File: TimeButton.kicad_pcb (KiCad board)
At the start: 2 copper layers, 3 parts, among them P1 USB_C_Plug_USB2.0, U1 PIC18F15Q41-I/SS, U2 FT231XS

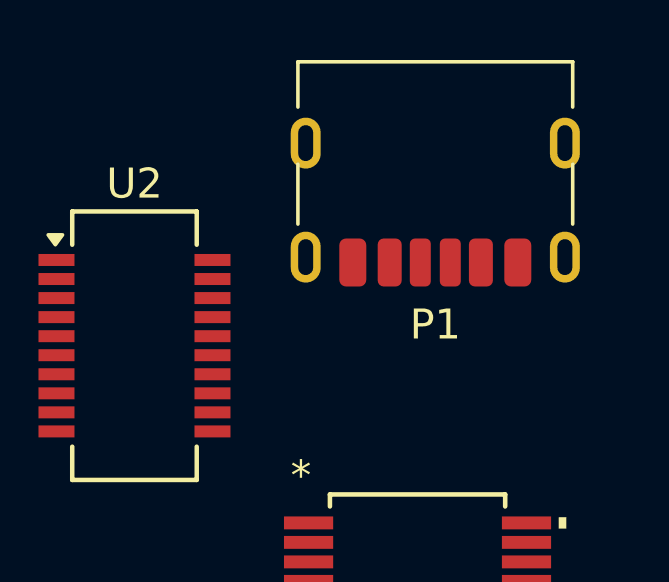
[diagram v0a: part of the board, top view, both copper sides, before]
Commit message: Changed USB_C connector from 6Pin to 16Pin
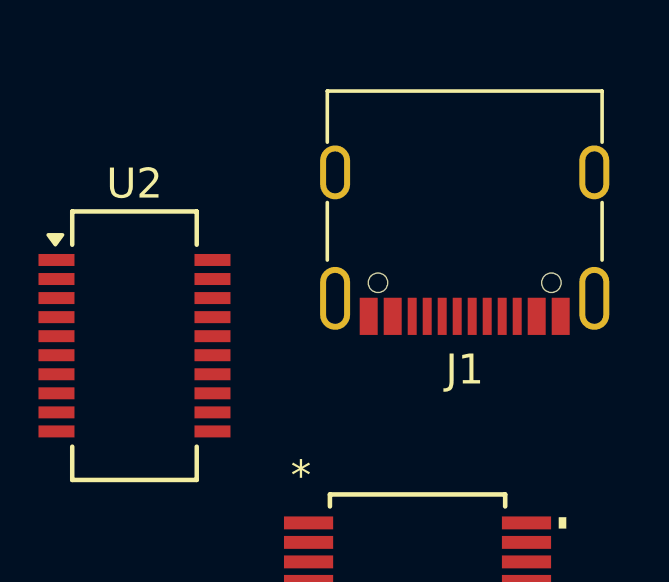
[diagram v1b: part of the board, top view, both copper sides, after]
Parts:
- removed P1: USB_C_Plug_USB2.0, Connector_USB:USB_C_Receptacle_HRO_TYPE-C-31-M-17
- added J1: USB_C_Receptacle_USB2.0_16P, Connector_USB:USB_C_Receptacle_G-Switch_GT-USB-7010ASV, F.Cu at (42.5, 30.3)

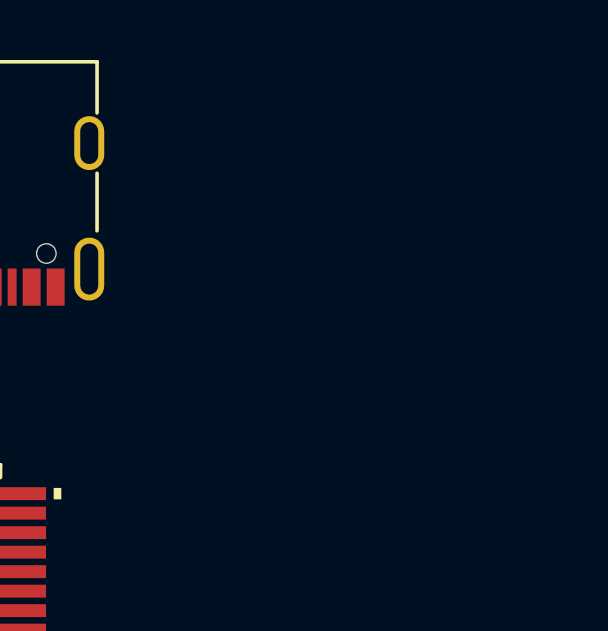
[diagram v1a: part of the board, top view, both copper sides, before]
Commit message: Added LEDs
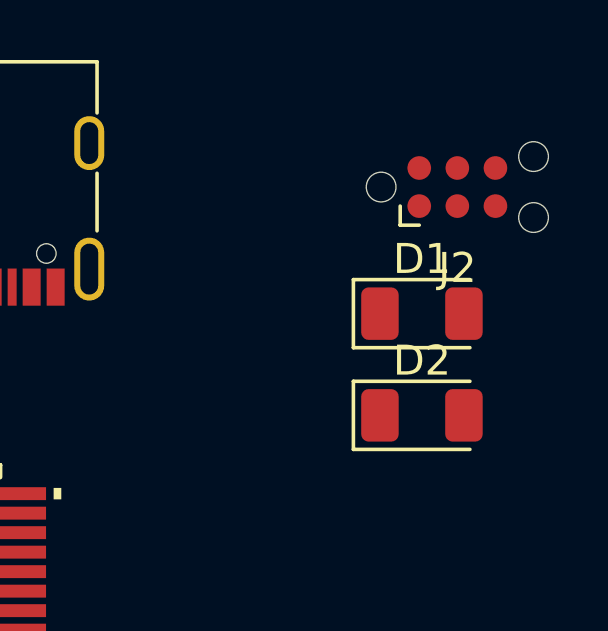
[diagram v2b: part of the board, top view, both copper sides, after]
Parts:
- added D1: 0603-Blue, LED_SMD:LED_1206_3216Metric, F.Cu at (57.9, 34.9)
- added D2: 0603-Green, LED_SMD:LED_1206_3216Metric, F.Cu at (57.9, 38.3)
- added J2: Conn_ARM_SWD_TagConnect_TC2030-NL, Connector:Tag-Connect_TC2030-IDC-NL_2x03_P1.27mm_Vertical, F.Cu at (59.1, 30.7)

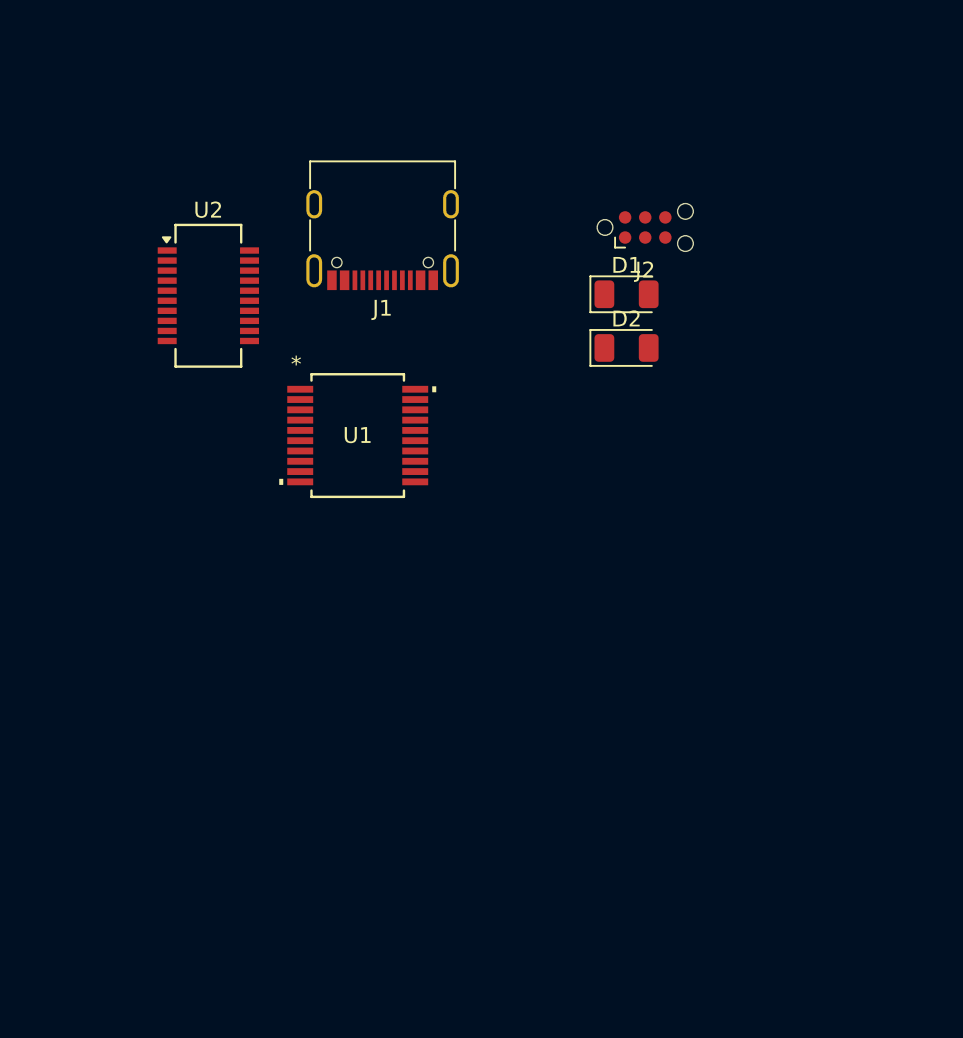
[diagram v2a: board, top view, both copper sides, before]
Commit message: Added TagConnect connections in the schematic
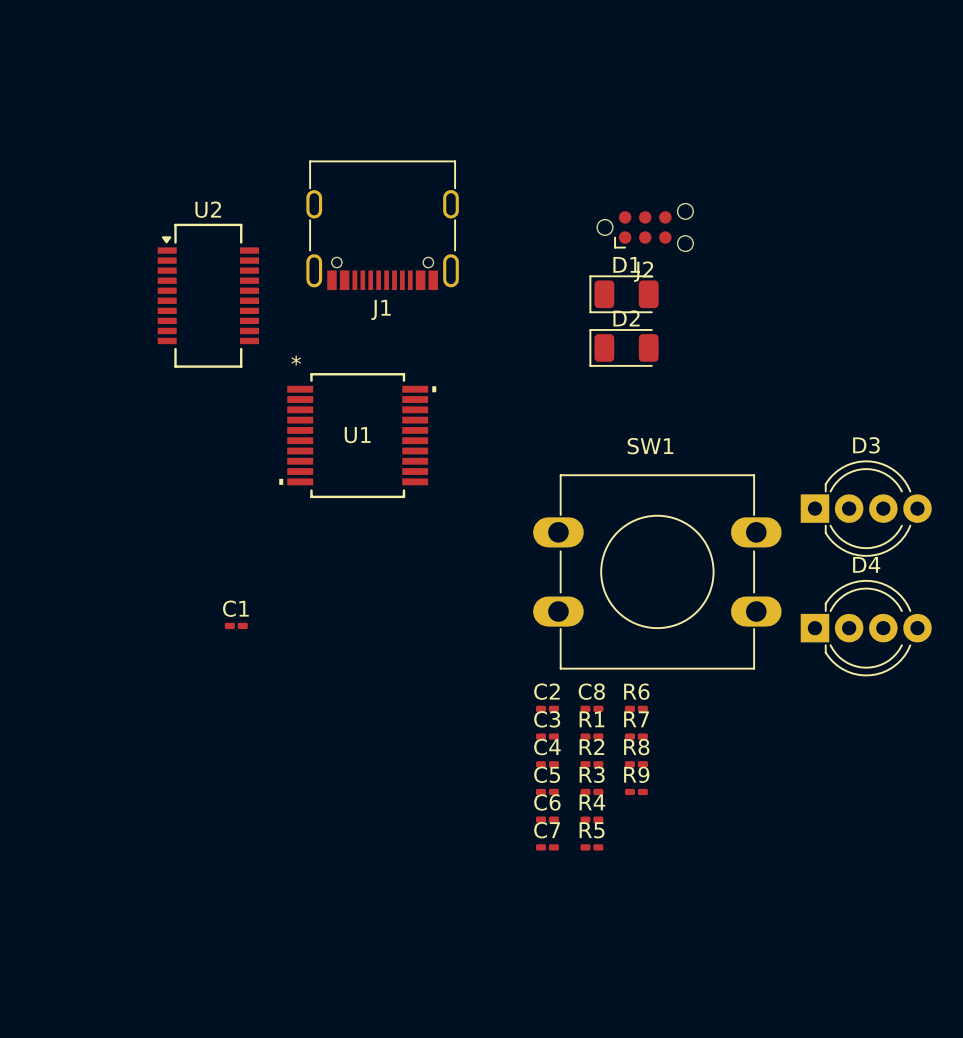
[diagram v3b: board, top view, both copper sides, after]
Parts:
- added C1: 10nF, Capacitor_SMD:C_0201_0603Metric_Pad0.64x0.40mm_HandSolder, F.Cu at (33.2, 55.9)
- added C2: 4.7uF, Capacitor_SMD:C_0201_0603Metric_Pad0.64x0.40mm_HandSolder, F.Cu at (52.9, 61.1)
- added C3: 10nF, Capacitor_SMD:C_0201_0603Metric_Pad0.64x0.40mm_HandSolder, F.Cu at (52.9, 62.9)
- added C4: 100nF, Capacitor_SMD:C_0201_0603Metric_Pad0.64x0.40mm_HandSolder, F.Cu at (52.9, 64.6)
- added C5: 4.7uF, Capacitor_SMD:C_0201_0603Metric_Pad0.64x0.40mm_HandSolder, F.Cu at (52.9, 66.4)
- added C6: 4.7uF, Capacitor_SMD:C_0201_0603Metric_Pad0.64x0.40mm_HandSolder, F.Cu at (52.9, 68.1)
- added C7: 100nF, Capacitor_SMD:C_0201_0603Metric_Pad0.64x0.40mm_HandSolder, F.Cu at (52.9, 69.9)
- added C8: 10nF, Capacitor_SMD:C_0201_0603Metric_Pad0.64x0.40mm_HandSolder, F.Cu at (55.7, 61.1)
- added D3: LED_RAGB, LED_THT:LED_D5.0mm-4_RGB_Wide_Pins, F.Cu at (69.8, 48.5)
- added D4: LED_RAGB, LED_THT:LED_D5.0mm-4_RGB_Wide_Pins, F.Cu at (69.8, 56.0)
- added R1: 10k, Resistor_SMD:R_0201_0603Metric_Pad0.64x0.40mm_HandSolder, F.Cu at (55.7, 62.9)
- added R2: 5.1k, Resistor_SMD:R_0201_0603Metric_Pad0.64x0.40mm_HandSolder, F.Cu at (55.7, 64.6)
- added R3: 27R, Resistor_SMD:R_0201_0603Metric_Pad0.64x0.40mm_HandSolder, F.Cu at (55.7, 66.4)
- added R4: 27R, Resistor_SMD:R_0201_0603Metric_Pad0.64x0.40mm_HandSolder, F.Cu at (55.7, 68.1)
- added R5: 1M, Resistor_SMD:R_0201_0603Metric_Pad0.64x0.40mm_HandSolder, F.Cu at (55.7, 69.9)
- added R6: 5.1k, Resistor_SMD:R_0201_0603Metric_Pad0.64x0.40mm_HandSolder, F.Cu at (58.5, 61.1)
- added R7: 100R, Resistor_SMD:R_0201_0603Metric_Pad0.64x0.40mm_HandSolder, F.Cu at (58.5, 62.9)
- added R8: 50R, Resistor_SMD:R_0201_0603Metric_Pad0.64x0.40mm_HandSolder, F.Cu at (58.5, 64.6)
- added R9: 50R, Resistor_SMD:R_0201_0603Metric_Pad0.64x0.40mm_HandSolder, F.Cu at (58.5, 66.4)
- added SW1: SW_Push, Button_Switch_THT:SW_PUSH-12mm, F.Cu at (53.6, 50.0)
- J2: value Conn_ARM_SWD_TagConnect_TC2030-NL -> TagConnect
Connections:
- J2 pad 1: unconnected-(J2-VCC-Pad1) -> 5V
- J2 pad 2: unconnected-(J2-SWDIO-Pad2) -> SWDIO
- J2 pad 3: unconnected-(J2-~{RESET}-Pad3) -> nRST
- J2 pad 4: unconnected-(J2-SWCLK-Pad4) -> SWCLK
- J2 pad 5: unconnected-(J2-GND-Pad5) -> GND
- U1 pad 1: unconnected-(U1-VDD-Pad1) -> 5V
- U1 pad 18: unconnected-(U1-RA1/ICSPCLK-Pad18) -> SWCLK
- U1 pad 19: unconnected-(U1-RA0/ICSPDAT-Pad19) -> SWDIO
- U1 pad 20: unconnected-(U1-VSS-Pad20) -> GND
- U1 pad 4: unconnected-(U1-*MCLR/VPP/RA3-Pad4) -> nRST

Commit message: Layout v1.0
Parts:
- removed C1: 10nF, Capacitor_SMD:C_0201_0603Metric_Pad0.64x0.40mm_HandSolder
- added J3: Conn_01x05_Pin, Connector_PinHeader_2.00mm:PinHeader_1x05_P2.00mm_Vertical, F.Cu at (36.1, 55.0)
- added J4: Conn_01x03_Pin, Connector_PinHeader_2.00mm:PinHeader_1x03_P2.00mm_Vertical, F.Cu at (62.7, 42.6)
- C2, C3, C4, C5, C6, C7, C8: footprint Capacitor_SMD:C_0201_0603Metric_Pad0.64x0.40mm_HandSolder -> Capacitor_SMD:C_0805_2012Metric_Pad1.18x1.45mm_HandSolder
- D1, D2: footprint LED_SMD:LED_1206_3216Metric -> LED_SMD:LED_0805_2012Metric_Pad1.15x1.40mm_HandSolder
- R1, R2, R3, R4, R5, R6, R7, R8, R9: footprint Resistor_SMD:R_0201_0603Metric_Pad0.64x0.40mm_HandSolder -> Resistor_SMD:R_0805_2012Metric_Pad1.20x1.40mm_HandSolder
- moved R5 39.9 mm to (51.0, 30.3), turned to -90 degrees
- moved J2 36.9 mm to (42.1, 63.4)
- moved C6 33.3 mm to (40.5, 37.2), turned to -135 degrees
- moved R6 31.7 mm to (37.8, 37.1), turned to -135 degrees
- moved C8 31.6 mm to (48.9, 30.3), turned to 90 degrees
- moved R7 31.0 mm to (53.1, 32.4), turned to -90 degrees
- moved R4 31.0 mm to (41.2, 40.7), turned to 90 degrees
- moved C5 30.3 mm to (44.6, 37.2), turned to -45 degrees
- moved R2 28.4 mm to (47.6, 37.4), turned to -45 degrees
- moved R3 28.2 mm to (43.9, 40.7), turned to 90 degrees
- moved R1 27.0 mm to (37.5, 43.0), turned to 45 degrees
- moved R9 24.2 mm to (50.9, 43.5), turned to 90 degrees
- moved C4 22.8 mm to (37.1, 48.2), turned to 180 degrees
- moved C3 20.2 mm to (37.1, 50.2), turned to 180 degrees
- moved C7 20.0 mm to (47.0, 50.8), turned to -90 degrees
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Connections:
- C2 pad 1: +5V -> 5V
- C3 pad 1: +5V -> 5V
- C4 pad 1: +5V -> 5V
- SW1 pad 1: unconnected-(SW1-Pad1) -> GND
- SW1 pad 2: unconnected-(SW1-Pad2) -> Net-(U1-RA2)
- U1 pad 10: unconnected-(U1-RB7-Pad10) -> Net-(J3-Pin_5)
- U1 pad 12: unconnected-(U1-RB5-Pad12) -> Net-(J4-Pin_2)
- U1 pad 14: unconnected-(U1-RC2-Pad14) -> PWM_B
- U1 pad 15: unconnected-(U1-RC1-Pad15) -> PWM_G
- U1 pad 16: unconnected-(U1-RC0-Pad16) -> PWM_R
- U1 pad 17: unconnected-(U1-RA2-Pad17) -> Net-(U1-RA2)
- U1 pad 6: unconnected-(U1-RC4-Pad6) -> Net-(J3-Pin_2)
- U1 pad 7: unconnected-(U1-RC3-Pad7) -> Net-(J3-Pin_3)
- U1 pad 9: unconnected-(U1-RC7-Pad9) -> Net-(J3-Pin_4)
- U2 pad 15: +5V -> 5V
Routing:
- net 3.3V: track 0.00 -> 69.5 mm
- net 5V: track 0.00 -> 55.5 mm
- net Net-(J4-Pin_2): track 0.00 -> 49.1 mm
- net PWM_B: track 0.00 -> 43.6 mm
- net PWM_G: track 0.00 -> 41.3 mm
- net PWM_R: track 0.00 -> 28.2 mm
- net nRST: track 0.00 -> 15.7 mm
- net GND: track 0.00 -> 12.1 mm, vias 0 -> 6
- net SWDIO: track 0.00 -> 11.1 mm
- net SWCLK: track 0.00 -> 9.73 mm
- net Net-(C6-Pad1): track 0.00 -> 8.99 mm
- net Net-(C5-Pad1): track 0.00 -> 8.83 mm
- net Net-(U2-USBDM): track 0.00 -> 7.26 mm
- net Net-(U2-USBDP): track 0.00 -> 7.21 mm
- net Net-(U2-~{RESET}): track 0.00 -> 5.12 mm
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- added copper zone on B.Cu, net GND
- added copper zone on F.Cu, net GND
- added copper zone on F.Cu, net Net-(J1-SHIELD)
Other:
- board outline added: 31.9 x 40 mm

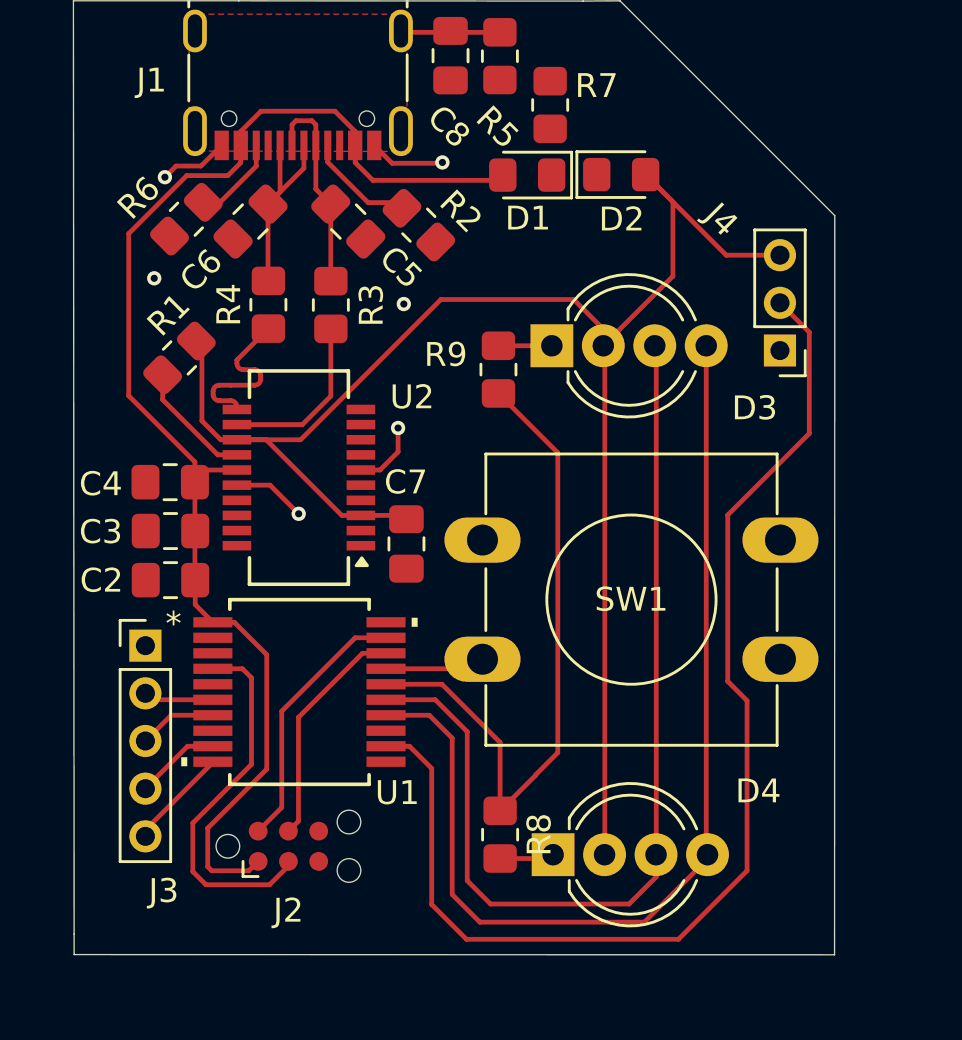
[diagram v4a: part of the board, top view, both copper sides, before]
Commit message: Added UART connection to FT231XS + changed some pin outputs as a result to fit it into the design
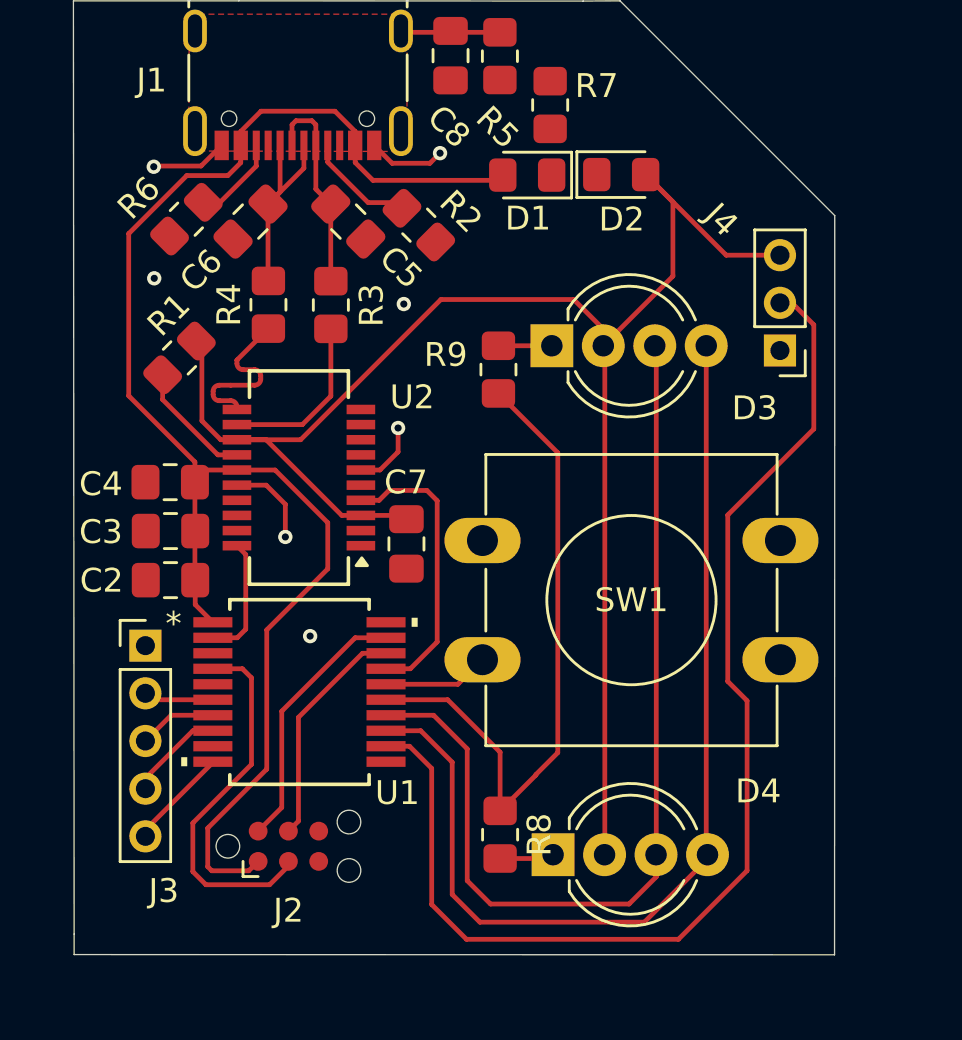
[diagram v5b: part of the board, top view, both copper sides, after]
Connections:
- SW1 pad 2: Net-(U1-RA2) -> Net-(U1-RC0)
- U1 pad 13: unconnected-(U1-RB4-Pad13) -> PWM_B
- U1 pad 14: PWM_B -> PWM_G
- U1 pad 15: PWM_G -> PWM_R
- U1 pad 16: PWM_R -> Net-(U1-RC0)
- U1 pad 17: Net-(U1-RA2) -> FT231XS_UART_TX
- U1 pad 2: unconnected-(U1-RA5-Pad2) -> FT231XS_UART_RX
- U1 pad 8: unconnected-(U1-RC6-Pad8) -> Net-(J3-Pin_4)
- U1 pad 9: Net-(J3-Pin_4) -> unconnected-(U1-RC7-Pad9)
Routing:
- net FT231XS_UART_TX: track 0.00 -> 12.1 mm
- net 5V: track 55.5 -> 64.0 mm
- net FT231XS_UART_RX: track 0.00 -> 5.18 mm
- net Net-(U1-RC0): track 0.00 -> 5.04 mm
- net Net-(U1-RA2): track 4.21 -> 0.00 mm
- net GND: track 12.1 -> 13.1 mm, vias 6 -> 7
- net PWM_B: track 43.6 -> 42.7 mm
- net PWM_G: track 41.3 -> 40.6 mm
- net Net-(J3-Pin_4): track 3.57 -> 4.09 mm
- net PWM_R: track 28.2 -> 27.7 mm
